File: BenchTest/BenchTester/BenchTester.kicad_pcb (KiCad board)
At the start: 2 copper layers, 8 parts, among them J1 Conn_01x01_Socket, J2 Conn_01x01_Socket, J3 Conn_01x01_Socket, J5 Conn_01x01_Socket, J6 Conn_01x01_Socket, J7 Conn_01x01_Socket, J8 Conn_01x01_Socket, J9 Conn_01x01_Socket

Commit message: Basic Incomplete placement
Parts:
- added C1: C, Capacitor_SMD:C_0805_2012Metric, F.Cu at (108.6, 111.0)
- added C2: C, Capacitor_SMD:C_0805_2012Metric, F.Cu at (108.6, 114.0)
- added C3: C, Capacitor_SMD:C_0805_2012Metric, F.Cu at (108.6, 117.0)
- added C5: C, Capacitor_SMD:C_0805_2012Metric, F.Cu at (108.6, 120.1)
- added D1: D_AAK, Library:TO-252-2_SBR20M150D1Q, F.Cu at (91.9, 62.8)
- added D2: D_AAK, Library:TO-252-2_SBR20M150D1Q, F.Cu at (91.1, 75.7)
- added D3: D_AAK, Library:TO-252-2_SBR20M150D1Q, F.Cu at (88.7, 86.9)
- added D4: D_AAK, Library:TO-252-2_SBR20M150D1Q, F.Cu at (89.2, 98.2)
- added D5: D_AAK, Library:TO-252-2_SBR20M150D1Q, F.Cu at (89.3, 108.7)
- added D7: D_AAK, Library:TO-252-2_SBR20M150D1Q, F.Cu at (87.6, 119.3)
- added H1: MountingHole, MountingHole:MountingHole_3.2mm_M3, F.Cu at (110.4, 81.7)
- added H2: MountingHole, MountingHole:MountingHole_3.2mm_M3, F.Cu at (110.4, 89.7)
- added H3: MountingHole, MountingHole:MountingHole_3.2mm_M3, F.Cu at (110.4, 97.6)
- added H4: MountingHole, MountingHole:MountingHole_3.2mm_M3_Pad, F.Cu at (110.4, 105.5)
- added J4: Conn_01x02_Socket, Connector_PinHeader_2.54mm:PinHeader_1x02_P2.54mm_Vertical, F.Cu at (119.0, 121.4)
- added Q1: Q_NMOS_GDS, Package_TO_SOT_THT:TO-220-3_Vertical, F.Cu at (185.0, 108.4)
- added Q2: Q_NMOS_GDS, Package_TO_SOT_THT:TO-220-3_Vertical, F.Cu at (184.4, 82.7)
- added Q3: Q_NMOS_GDS, Package_TO_SOT_THT:TO-220-3_Vertical, F.Cu at (211.5, 108.8)
- added Q5: Q_NMOS_GDS, Package_TO_SOT_THT:TO-220-3_Vertical, F.Cu at (210.7, 81.9)
- added R1: 100k, Resistor_SMD:R_0402_1005Metric, F.Cu at (112.3, 110.5)
- added R10: 100k, Resistor_SMD:R_0402_1005Metric, F.Cu at (115.2, 118.5)
- added R2: 33, Resistor_SMD:R_0402_1005Metric, F.Cu at (112.3, 112.5)
- added R3: 100k, Resistor_SMD:R_0402_1005Metric, F.Cu at (112.3, 114.5)
- added R4: 33, Resistor_SMD:R_0402_1005Metric, F.Cu at (112.3, 116.5)
- added R5: 33, Resistor_SMD:R_0402_1005Metric, F.Cu at (112.3, 118.5)
- added R6: 33, Resistor_SMD:R_0402_1005Metric, F.Cu at (115.2, 110.5)
- added R7: 100k, Resistor_SMD:R_0402_1005Metric, F.Cu at (115.2, 112.5)
- added R8: 100k, Resistor_SMD:R_0402_1005Metric, F.Cu at (115.2, 114.5)
- added R9: 100k, Resistor_SMD:R_0402_1005Metric, F.Cu at (115.2, 116.5)
- added U1: ~, Package_TO_SOT_SMD:SOT-23-6_Handsoldering, F.Cu at (119.6, 112.0)
- added U2: ~, Package_TO_SOT_SMD:SC-74A-5_1.55x2.9mm_P0.95mm, F.Cu at (125.2, 111.9)
- added U3: ~, Package_TO_SOT_SMD:SC-74A-5_1.55x2.9mm_P0.95mm, F.Cu at (125.2, 116.5)
- added U4: ~, Package_TO_SOT_SMD:SOT-23-6_Handsoldering, F.Cu at (119.6, 116.8)

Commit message: Initial Placement
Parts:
- H4: footprint MountingHole:MountingHole_3.2mm_M3_Pad -> MountingHole:MountingHole_3.2mm_M3
- moved D7 137.1 mm to (213.7, 65.3)
- moved R4 124.9 mm to (230.9, 77.2)
- moved C3 124.7 mm to (226.0, 74.8)
- moved R3 120.9 mm to (224.9, 70.4)
- moved C5 116.6 mm to (225.2, 121.2)
- moved R10 115.3 mm to (230.3, 126.0)
- moved D4 114.4 mm to (203.7, 99.7)
- moved D2 113.2 mm to (203.7, 87.7)
- moved R9 109.3 mm to (224.5, 112.4)
- moved U4 107.8 mm to (218.8, 74.5)
- moved R5 107.2 mm to (219.3, 125.6)
- moved D3 100.3 mm to (188.3, 99.5)
- moved D1 99.3 mm to (188.2, 87.2)
- moved U3 93.0 mm to (218.2, 118.2)
- moved D5 90.8 mm to (169.5, 65.9)
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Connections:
- J5 pad 1: /EBUS -> /SBUS

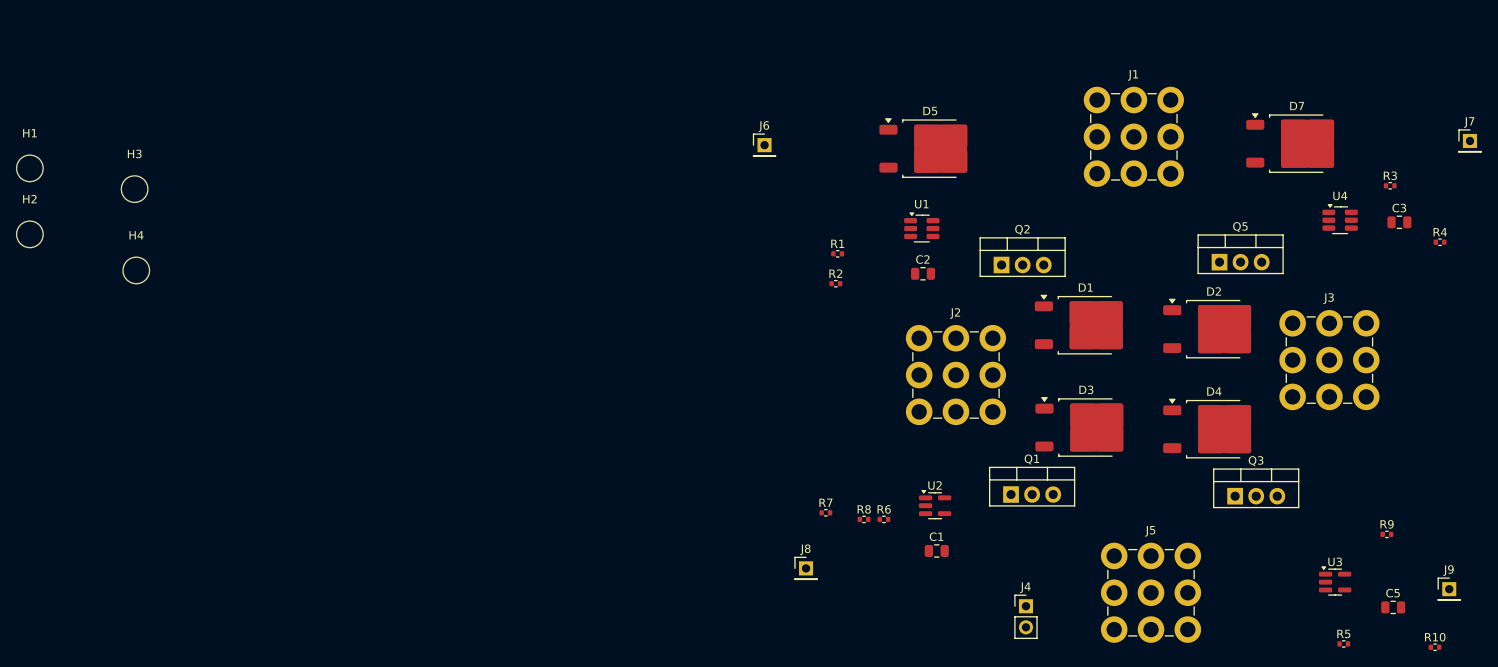
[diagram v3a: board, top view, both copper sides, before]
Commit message: Grouping Near Complete
Grouping of components is close to complete. Next is placement near
respective other groups. Need Full Footprint for FET with heatsink
before completing that exercise.
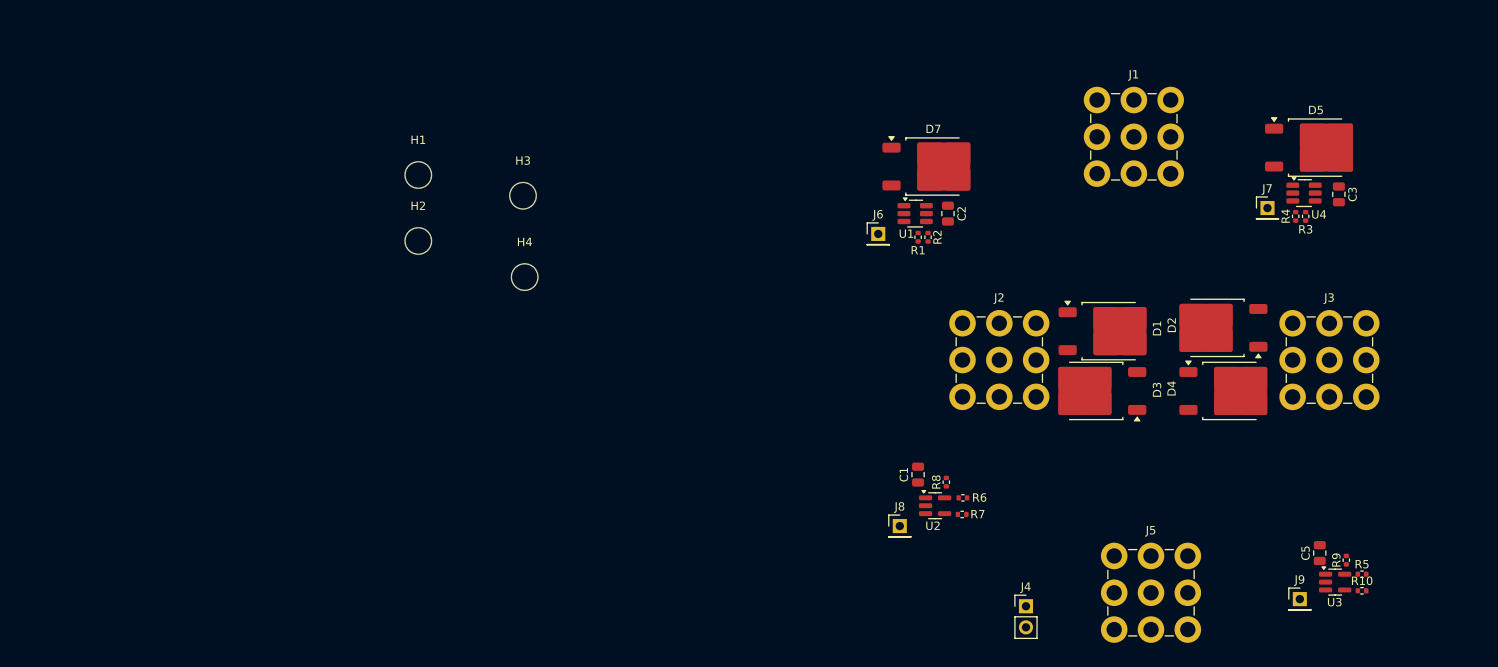
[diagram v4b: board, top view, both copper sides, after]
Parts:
- removed Q1, Q2, Q3, Q5: Q_NMOS_GDS, Package_TO_SOT_THT:TO-220-3_Vertical
- moved H3 46.8 mm to (120.4, 71.6)
- moved H1 46.8 mm to (107.8, 69.1)
- moved H2 46.8 mm to (107.8, 77.0)
- moved H4 46.8 mm to (120.6, 81.4)
- moved D5 46.5 mm to (215.9, 65.8)
- moved D7 43.9 mm to (169.8, 68.1)
- moved J7 25.7 mm to (210.1, 73.1)
- moved J9 18.0 mm to (214.0, 120.2)
- moved R4 17.7 mm to (213.5, 74.1), turned to 90 degrees
- moved J6 17.4 mm to (163.2, 76.2)
- moved R7 16.4 mm to (173.3, 110.0)
- moved R2 12.4 mm to (169.2, 76.6), turned to -90 degrees
- moved J8 12.4 mm to (165.8, 111.4)
- moved R10 11.1 mm to (221.5, 119.2)
- moved C5 11.0 mm to (216.4, 114.7), turned to 90 degrees
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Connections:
- C3 pad 2: /Motor0 -> /Motor1

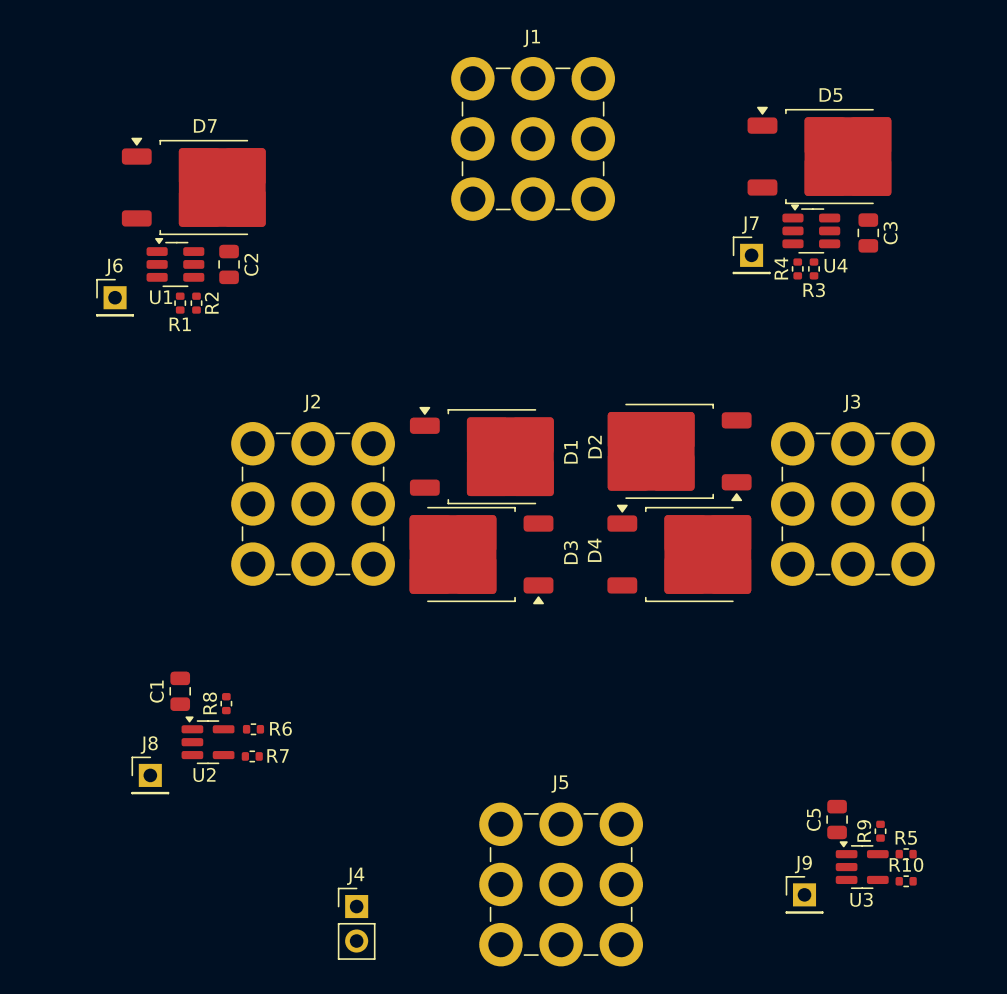
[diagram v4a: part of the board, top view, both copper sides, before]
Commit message: Footprint assignment
Footprint assignment for Fets.
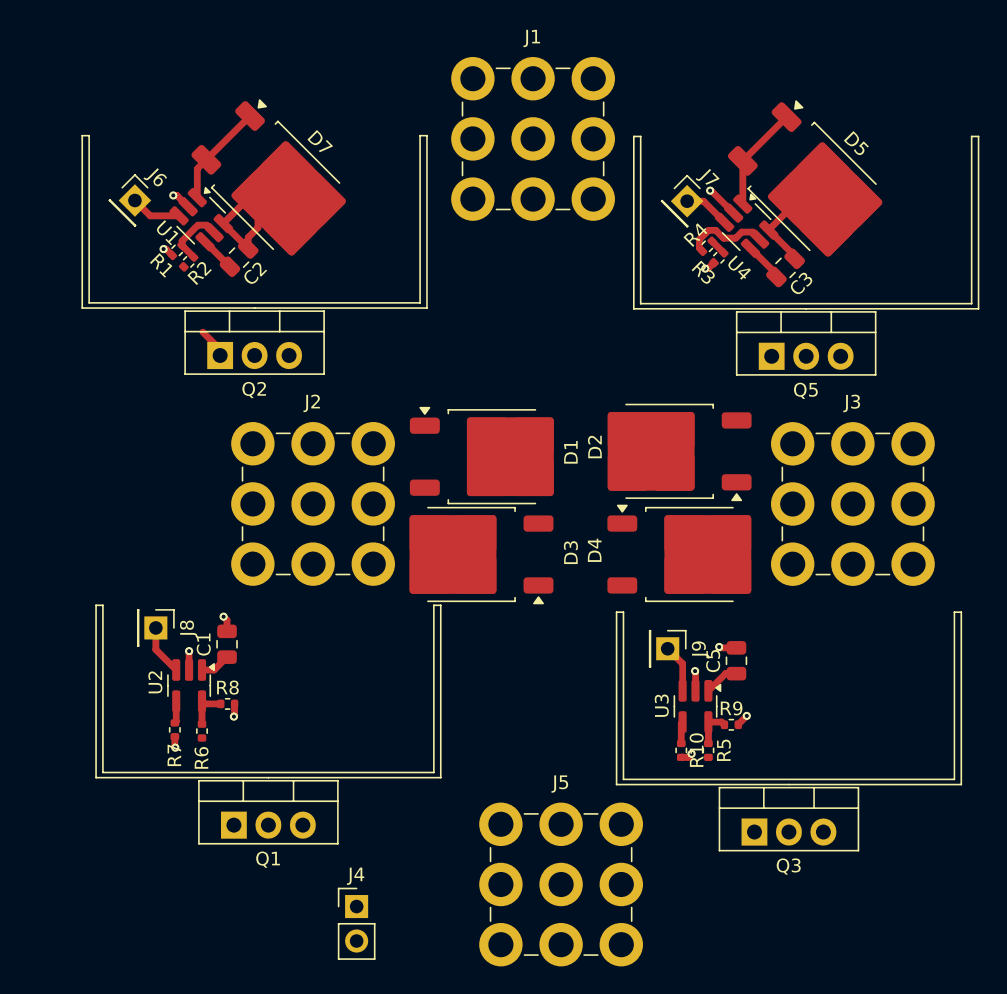
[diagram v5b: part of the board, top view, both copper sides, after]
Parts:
- added Q1: Q_NMOS_GDS, Library:TO-220-3-HeatSinked, F.Cu at (174.5, 114.6)
- added Q2: Q_NMOS_GDS, Library:TO-220-3-HeatSinked, F.Cu at (173.5, 80.0)
- added Q3: Q_NMOS_GDS, Library:TO-220-3-HeatSinked, F.Cu at (212.9, 115.1)
- added Q5: Q_NMOS_GDS, Library:TO-220-3-HeatSinked, F.Cu at (214.1, 80.1)
- moved J9 20.7 mm to (203.9, 102.1), turned to -90 degrees
- moved R10 19.2 mm to (204.9, 109.6), turned to -90 degrees
- moved U3 17.1 mm to (206.0, 106.3), turned to -90 degrees
- moved R5 16.5 mm to (206.9, 109.6), turned to -90 degrees
- moved C5 13.9 mm to (209.0, 103.0)
- moved R9 13.5 mm to (208.6, 107.7), turned to 0 degrees
- moved J8 10.9 mm to (166.2, 100.5), turned to -90 degrees
- moved J6 7.31 mm to (164.7, 69.0), turned to -45 degrees
- moved R3 7.06 mm to (207.7, 73.3), turned to -135 degrees
- moved R4 6.87 mm to (206.8, 72.4), turned to 45 degrees
- moved C3 6.62 mm to (212.6, 74.0), turned to -135 degrees
- moved J7 6.20 mm to (205.4, 69.1), turned to -45 degrees
- moved R7 6.03 mm to (167.6, 108.0), turned to -90 degrees
- moved D7 5.26 mm to (175.1, 68.0), turned to -45 degrees
- moved C1 4.89 mm to (171.4, 101.7)
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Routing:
- net /Vdrive: track 0.00 -> 20.2 mm
- net GND: track 0.00 -> 14.4 mm, vias 0 -> 12
- net Net-(D7-K): track 0.00 -> 10.1 mm
- net Net-(U4-HO): track 0.00 -> 6.31 mm
- net Net-(D5-K): track 0.00 -> 6.05 mm
- net Net-(U1-HO): track 0.00 -> 4.60 mm
- net /G2: track 0.00 -> 4.08 mm
- net /G3: track 0.00 -> 3.72 mm
- net /G1: track 0.00 -> 3.72 mm
- net /G4: track 0.00 -> 3.56 mm
- net Net-(U2-OUT): track 0.00 -> 3.15 mm
- net /Motor1: track 0.00 -> 2.91 mm
- net Net-(U3-OUT): track 0.00 -> 2.84 mm
- net /Motor0: track 0.00 -> 2.60 mm
- net Net-(Q2-G): track 0.00 -> 2.25 mm
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
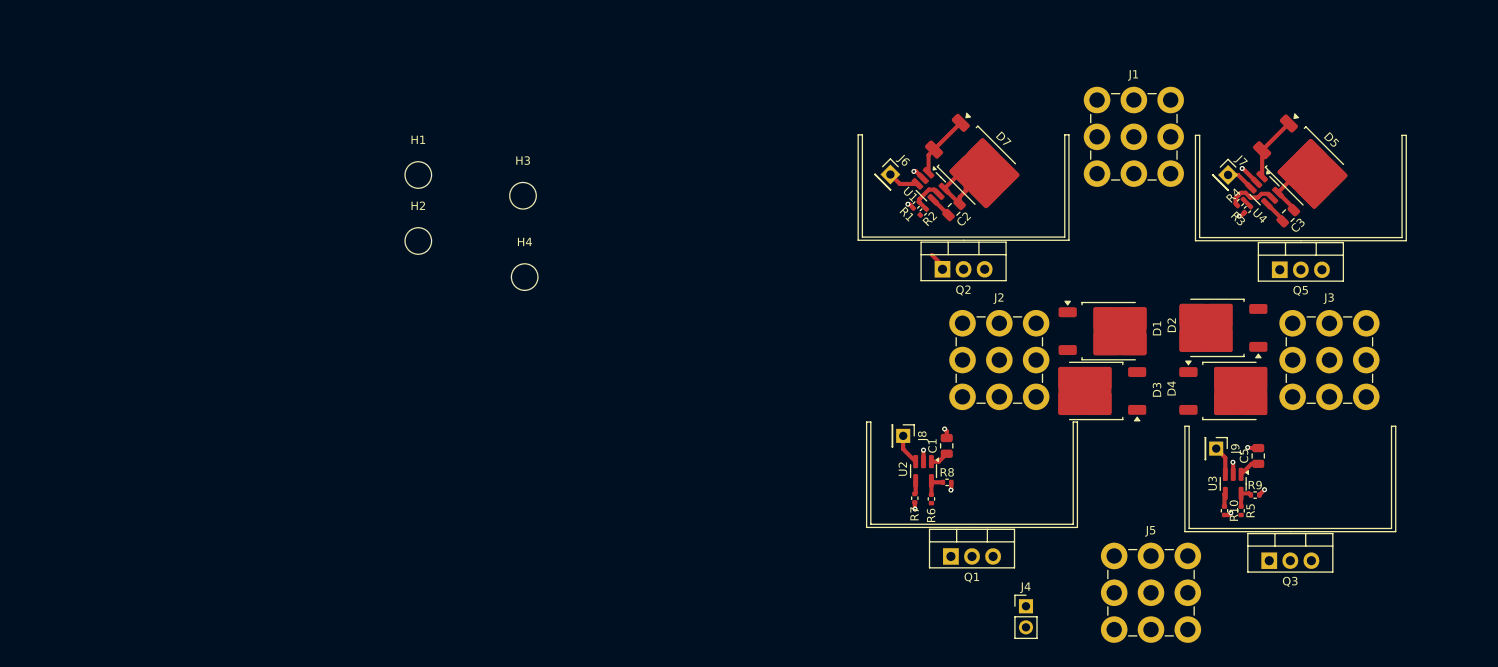
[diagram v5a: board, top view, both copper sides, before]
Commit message: Re-placement of positions to reduce trace length
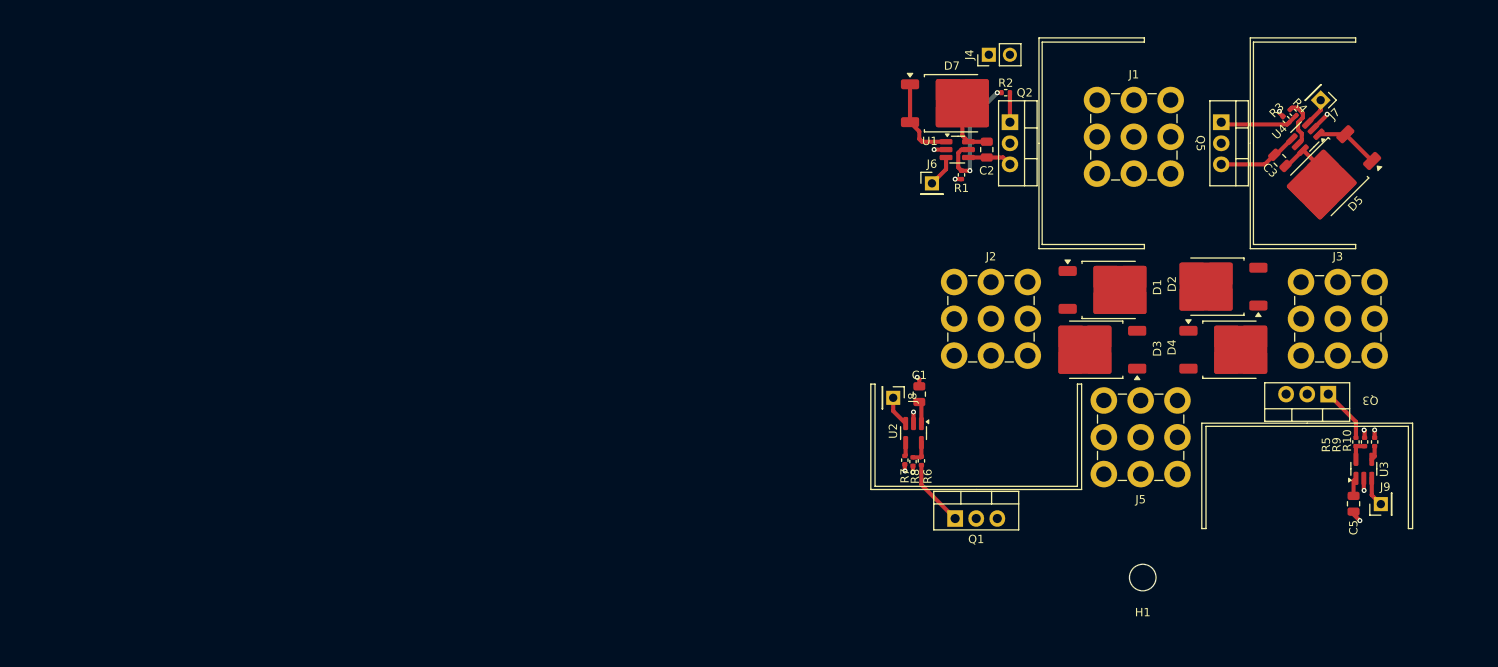
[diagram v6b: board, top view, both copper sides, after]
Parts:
- removed H2, H3, H4: MountingHole, MountingHole:MountingHole_3.2mm_M3
- moved H1 99.9 mm to (195.1, 117.6), turned to 180 degrees
- moved J4 66.6 mm to (176.5, 54.6), turned to 90 degrees
- moved J9 20.9 mm to (223.8, 108.8), turned to 90 degrees
- moved R10 19.9 mm to (223.0, 101.3), turned to 90 degrees
- moved Q3 19.3 mm to (214.9, 96.0), turned to 180 degrees
- moved J5 18.8 mm to (194.8, 100.7), turned to 180 degrees
- moved R2 17.5 mm to (178.6, 59.2), turned to 0 degrees
- moved Q5 17.4 mm to (205.0, 65.3), turned to -90 degrees
- moved R5 16.1 mm to (220.8, 101.3), turned to 90 degrees
- moved Q2 15.9 mm to (179.5, 65.3), turned to -90 degrees
- moved U3 15.8 mm to (221.7, 104.5), turned to 90 degrees
- moved R9 14.7 mm to (221.8, 101.3), turned to 90 degrees
- moved J7 14.3 mm to (216.5, 60.1), turned to -135 degrees
- moved C5 12.9 mm to (220.5, 108.7), turned to -90 degrees
- moved R4 12.6 mm to (213.2, 61.6), turned to -45 degrees
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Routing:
- net Net-(U1-HO): track 4.60 -> 16.0 mm, vias 0 -> 2
- net Net-(Q5-G): track 1.20 -> 9.58 mm
- net Net-(Q1-G): track 0.00 -> 8.12 mm
- net /Motor1: track 2.91 -> 9.79 mm
- net Net-(Q3-G): track 0.00 -> 6.63 mm
- net Net-(D7-K): track 10.1 -> 7.15 mm
- net /Vdrive: track 20.2 -> 23.1 mm
- net /Motor0: track 2.60 -> 5.34 mm
- net Net-(Q2-G): track 2.25 -> 3.56 mm

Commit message: Potential Layout
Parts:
- moved J4 66.4 mm to (216.4, 107.7), turned to 0 degrees
- moved H1 63.1 mm to (204.2, 55.1)
- moved D2 4.78 mm to (199.2, 82.5)
- moved D4 4.62 mm to (201.0, 90.2)
- moved J3 2.81 mm to (215.8, 86.4)
- moved D3 2.80 mm to (186.6, 90.2)
- moved D1 2.80 mm to (188.3, 82.9)
- moved J2 2.66 mm to (174.1, 86.4)
- moved C1 0.25 mm to (167.9, 95.5)
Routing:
- net GND: track 14.4 -> 215.9 mm
- net /Vdrive: track 23.1 -> 203.7 mm
- added copper zone on B.Cu, net /DBUS
- added copper zone on F.Cu, net /DBUS
- added copper zone on B.Cu, net /Motor0
- added copper zone on F.Cu, net /Motor0
- added copper zone on B.Cu, net /Motor1
- added copper zone on F.Cu, net /Motor1
- added copper zone on B.Cu, net /SBUS
- added copper zone on F.Cu, net /SBUS
